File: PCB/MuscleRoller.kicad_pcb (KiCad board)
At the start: 2 copper layers, 70 x 70 mm, 28 parts, among them J1 Conn_01x06_Male, J10 Conn_01x03_Male, J11 Conn_01x03_Male, J2 Conn_01x06_Male, J3 Screw_Terminal_01x02, J4 Conn_01x04_Male, J5 Conn_01x04_Male, J6 Conn_01x03_Male, J7 Conn_01x04_Male, J8 Conn_01x04_Male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

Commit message: GPIO pin updates complete
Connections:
- U2 pad 23: ESTOP -> MSX
- U2 pad 24: Net-(U2-Pad24) -> ESTOP
- U2 pad 36: Net-(U2-Pad36) -> STEPX
- U2 pad 37: Net-(U2-Pad37) -> DIRX
- U2 pad 5: DIRX -> Net-(U2-Pad5)
- U2 pad 6: STEPX -> Net-(U2-Pad6)
- U2 pad 7: MSX -> Net-(U2-Pad7)
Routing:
- net DIRX: track 6.88 -> 29.9 mm, vias 0 -> 1
- net STEPX: track 8.00 -> 28.9 mm, vias 0 -> 1
- net MSX: track 14.0 -> 21.1 mm, vias 0 -> 1
- net +12V: track 44.9 -> 45.8 mm
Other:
- board text added: "SAGE ROBOTS MUSCLE_ROLLER_1V0"

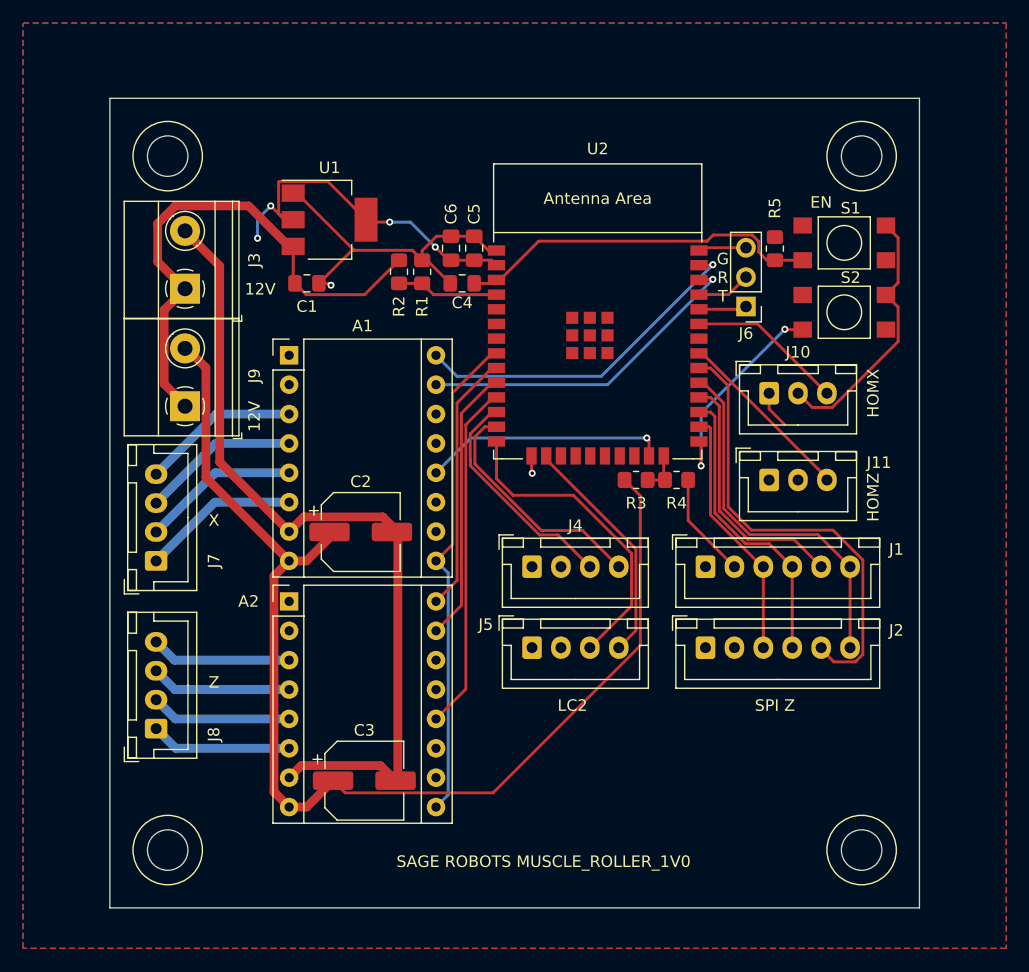
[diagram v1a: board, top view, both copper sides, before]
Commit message: R1 R2 labels were positioned incorrectly
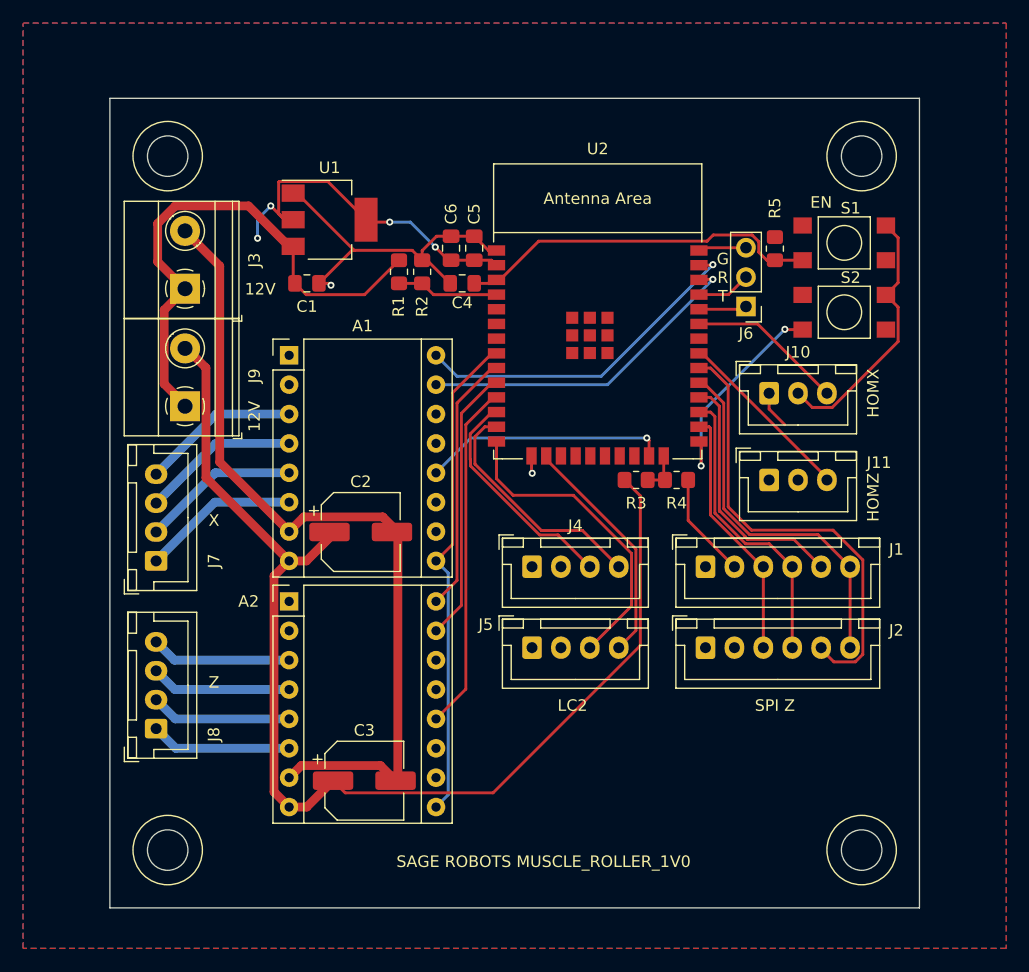
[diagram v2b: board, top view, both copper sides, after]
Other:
- net class Default removed

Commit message: Added LED for status, C7 for ESD protection
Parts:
- added C7: 100u, Capacitor_SMD:CP_Elec_6.3x7.7, F.Cu at (135.0, 87.0)
- added D1: LED, LED_SMD:LED_0805_2012Metric, F.Cu at (160.0, 90.0)
- added R6: 100, Resistor_SMD:R_0805_2012Metric_Pad1.20x1.40mm_HandSolder, F.Cu at (162.0, 90.0)
- S1, S2: footprint A4:TL3305AF160QG -> SageRobots:TL3305AF160QG
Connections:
- A1 pad 10: Net-(A1-Pad10) -> unconnected-(A1-Pad10)
- A1 pad 11: Net-(A1-Pad11) -> unconnected-(A1-Pad11)
- A1 pad 2: Net-(A1-Pad2) -> unconnected-(A1-Pad2)
- A2 pad 10: Net-(A2-Pad10) -> unconnected-(A2-Pad10)
- A2 pad 11: Net-(A2-Pad11) -> unconnected-(A2-Pad11)
- A2 pad 2: Net-(A2-Pad2) -> unconnected-(A2-Pad2)
- S1 pad 2: Net-(S1-Pad2) -> unconnected-(S1-Pad2)
- S1 pad 3: Net-(S1-Pad3) -> unconnected-(S1-Pad3)
- S2 pad 2: Net-(S2-Pad2) -> unconnected-(S2-Pad2)
- S2 pad 3: Net-(S2-Pad3) -> unconnected-(S2-Pad3)
- U2 pad 17: Net-(U2-Pad17) -> unconnected-(U2-Pad17)
- U2 pad 18: Net-(U2-Pad18) -> unconnected-(U2-Pad18)
- U2 pad 19: Net-(U2-Pad19) -> unconnected-(U2-Pad19)
- U2 pad 20: Net-(U2-Pad20) -> unconnected-(U2-Pad20)
- U2 pad 21: Net-(U2-Pad21) -> unconnected-(U2-Pad21)
- U2 pad 22: Net-(U2-Pad22) -> unconnected-(U2-Pad22)
- U2 pad 32: Net-(U2-Pad32) -> unconnected-(U2-Pad32)
- U2 pad 33: HOMX -> LED
- U2 pad 5: Net-(U2-Pad5) -> HOMX
- U2 pad 6: Net-(U2-Pad6) -> unconnected-(U2-Pad6)
- U2 pad 7: Net-(U2-Pad7) -> unconnected-(U2-Pad7)
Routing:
- net HOMX: track 13.6 -> 46.5 mm, vias 0 -> 1
- net LED: track 0.00 -> 31.1 mm
- net GND: track 140.1 -> 160.0 mm, vias 2 -> 4
- net +12V: track 45.8 -> 62.9 mm
- net Net-(D1-Pad1): track 0.00 -> 2.03 mm
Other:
- board text added: "SAGE ROBOTS ROBOROLLER_1V0"
- board text removed: "SAGE ROBOTS MUSCLE_ROLLER_1V0"
